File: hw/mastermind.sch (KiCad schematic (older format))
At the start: 16 parts, among them J1 CONN_01X03, SW1 R13-529, SW2 R13-529, SW3 R13-529, SW4 R13-529, U1 ESP32_THING, U2 LevelShifter

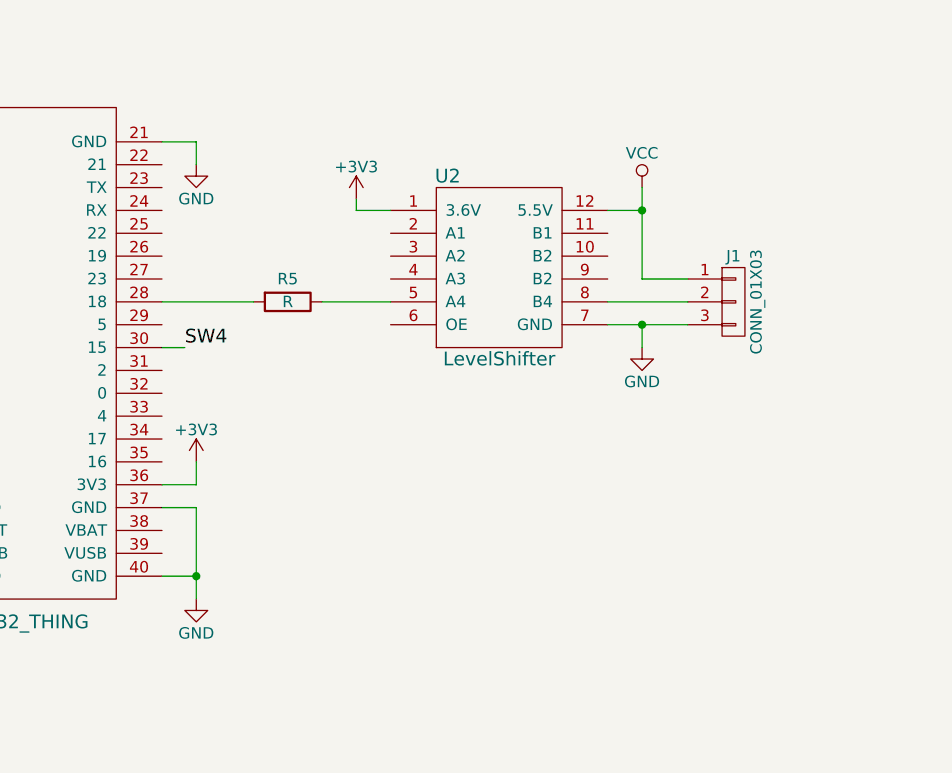
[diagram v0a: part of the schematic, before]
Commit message: Add power input header and a few corrections
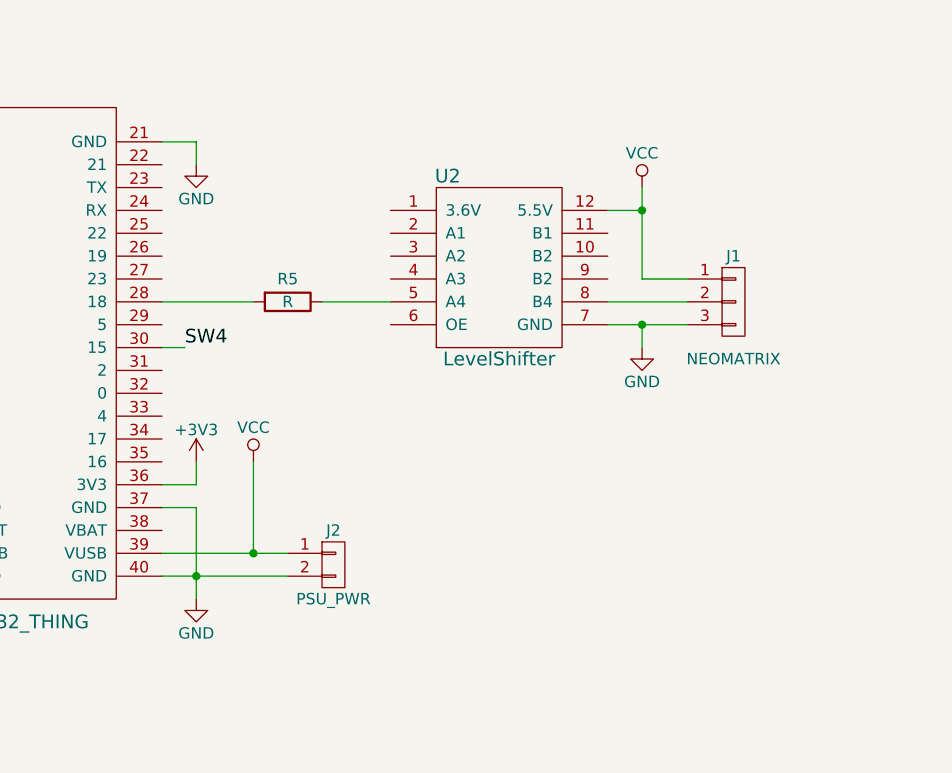
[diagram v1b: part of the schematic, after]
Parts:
- added J2: PSU_PWR, Pin_Headers:Pin_Header_Straight_1x02_Pitch2.00mm, symbol CONN_01X02
- J1: value CONN_01X03 -> NEOMATRIX
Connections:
- net +3V3: no longer U2.1 (3.6V)
- net GND: now also J2.2 (P2)
- net VCC: now also U1.39 (VUSB), J2.1 (P1)
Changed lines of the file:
@@
 $EndComp
 $Comp
-L +3V3 #PWR06
-U 1 1 59B667C6
-P 7100 3000
-F 0 "#PWR06" H 7100 2850 50  0001 C CNN
-F 1 "+3V3" H 7100 3140 50  0000 C CNN
-F 2 "" H 7100 3000 50  0001 C CNN
-F 3 "" H 7100 3000 50  0001 C CNN
-	1    7100 3000
-	1    0    0    -1
-$EndComp
-$Comp
-L GND #PWR07
+L GND #PWR06
 U 1 1 59B66A40
 P 8350 3650
-F 0 "#PWR07" H 8350 3400 50  0001 C CNN
+F 0 "#PWR06" H 8350 3400 50  0001 C CNN
 F 1 "GND" H 8350 3500 50  0000 C CNN
 F 2 "" H 8350 3650 50  0001 C CNN
@@
 $EndComp
 $Comp
-L GND #PWR08
+L GND #PWR07
 U 1 1 59B6725E
 P 4950 5100
-F 0 "#PWR08" H 4950 4850 50  0001 C CNN
+F 0 "#PWR07" H 4950 4850 50  0001 C CNN
 F 1 "GND" H 4950 4950 50  0000 C CNN
 F 2 "" H 4950 5100 50  0001 C CNN
@@
 $EndComp
 $Comp
-L +3V3 #PWR09
+L +3V3 #PWR08
 U 1 1 59B6737B
 P 4950 4250
-F 0 "#PWR09" H 4950 4100 50  0001 C CNN
+F 0 "#PWR08" H 4950 4100 50  0001 C CNN
 F 1 "+3V3" H 4950 4390 50  0000 C CNN
 F 2 "" H 4950 4250 50  0001 C CNN
@@
 $EndComp
 $Comp
-L GND #PWR010
+L GND #PWR09
 U 1 1 59B676EB
 P 6400 2850
-F 0 "#PWR010" H 6400 2600 50  0001 C CNN
+F 0 "#PWR09" H 6400 2600 50  0001 C CNN
 F 1 "GND" H 6400 2700 50  0000 C CNN
 F 2 "" H 6400 2850 50  0001 C CNN
@@
 P 8750 3450
 F 0 "J1" H 8750 3650 50  0000 C CNN
-F 1 "CONN_01X03" V 8850 3450 50  0000 C CNN
+F 1 "NEOMATRIX" H 8750 3200 50  0000 C CNN
 F 2 "Pin_Headers:Pin_Header_Straight_1x03_Pitch2.00mm" H 8750 3450 50  0001 C CNN
 F 3 "" H 8750 3450 50  0001 C CNN
@@
 $EndComp
 Wire Wire Line
-	6400 4650 6250 4650
+	6250 4650 6800 4650
 Wire Wire Line
 	6400 4350 6400 4750
@@
 Wire Wire Line
 	8350 3050 8200 3050
-Wire Wire Line
-	7250 3050 7100 3050
-Wire Wire Line
-	7100 3050 7100 3000
 Wire Wire Line
 	8350 3650 8350 3550
@@
 	4100 4850 4000 4850
 Connection ~ 4100 4150
+$Comp
+L VCC #PWR010
+U 1 1 59B7DB57
+P 6650 4150
+F 0 "#PWR010" H 6650 4000 50  0001 C CNN
+F 1 "VCC" H 6650 4300 50  0000 C CNN
+F 2 "" H 6650 4150 50  0001 C CNN
+F 3 "" H 6650 4150 50  0001 C CNN
+	1    6650 4150
+	1    0    0    -1
+$EndComp
+Wire Wire Line
+	6650 4150 6650 4550
+Wire Wire Line
+	6250 4550 6800 4550
+$Comp
+L CONN_01X02 J2
+U 1 1 59B7DDF1
+P 7000 4600
+F 0 "J2" H 7000 4750 50  0000 C CNN
+F 1 "PSU_PWR" H 7000 4450 50  0000 C CNN
+F 2 "Pin_Headers:Pin_Header_Straight_1x02_Pitch2.00mm" H 7000 4600 50  0001 C CNN
+F 3 "" H 7000 4600 50  0001 C CNN
+	1    7000 4600
+	1    0    0    -1
+$EndComp
+Connection ~ 6650 4550
 $EndSCHEMATC

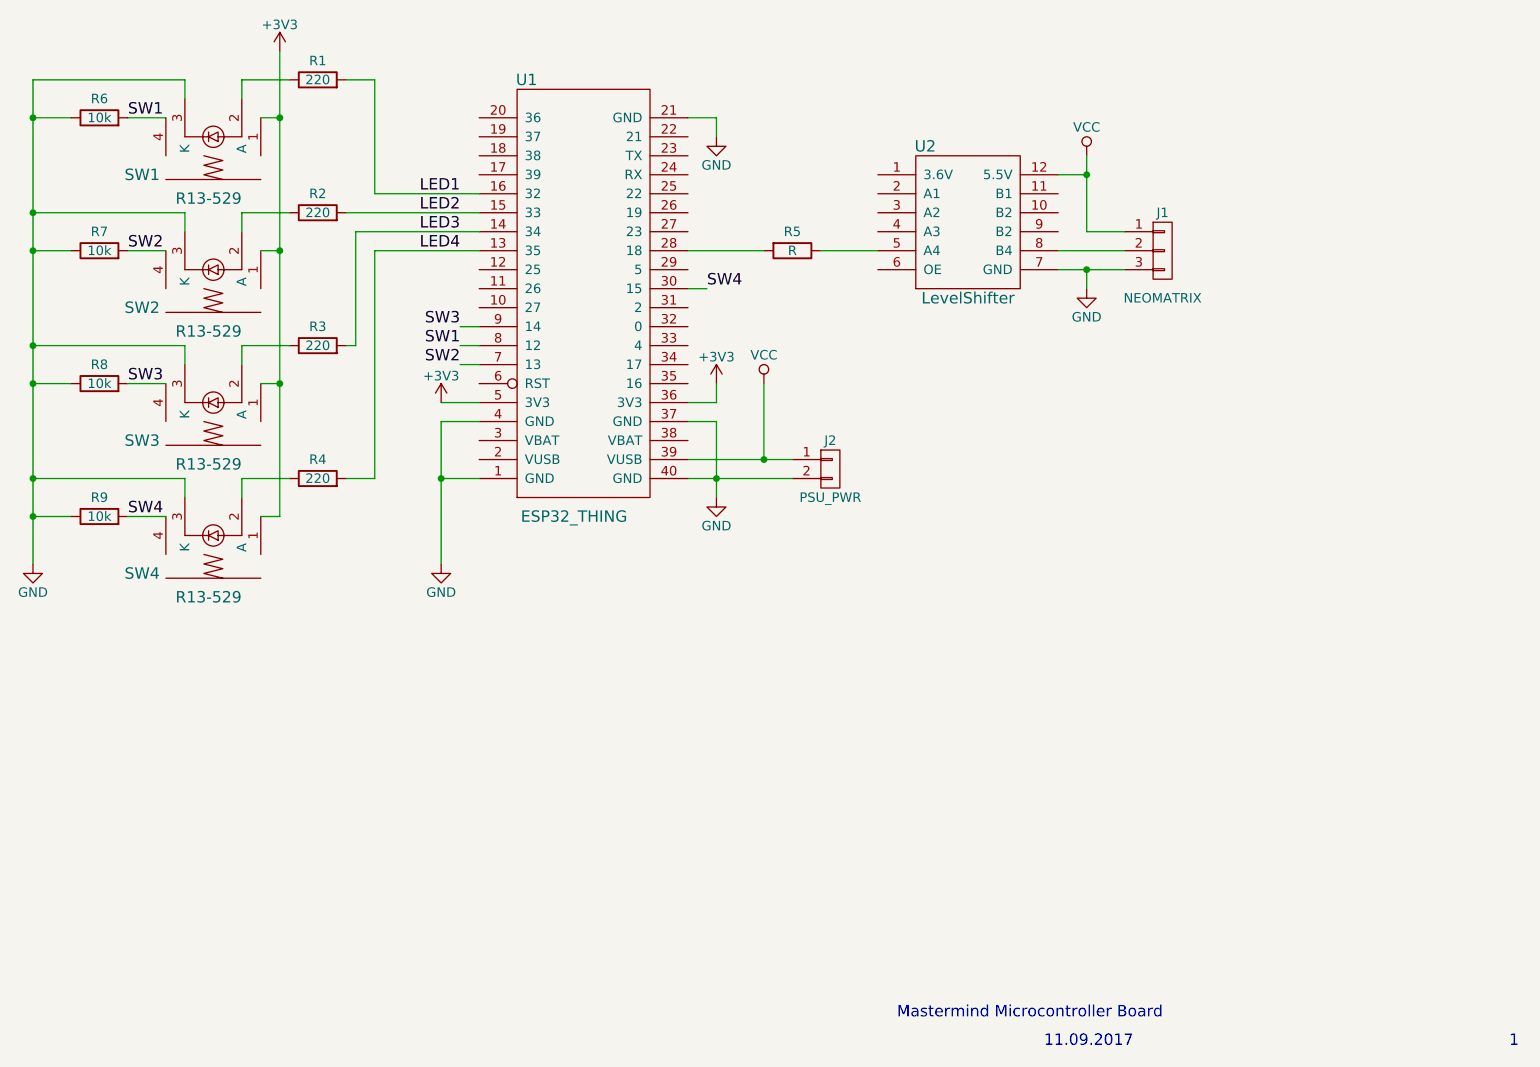
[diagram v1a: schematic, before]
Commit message: Redoing PCB design because there are a few mistakes
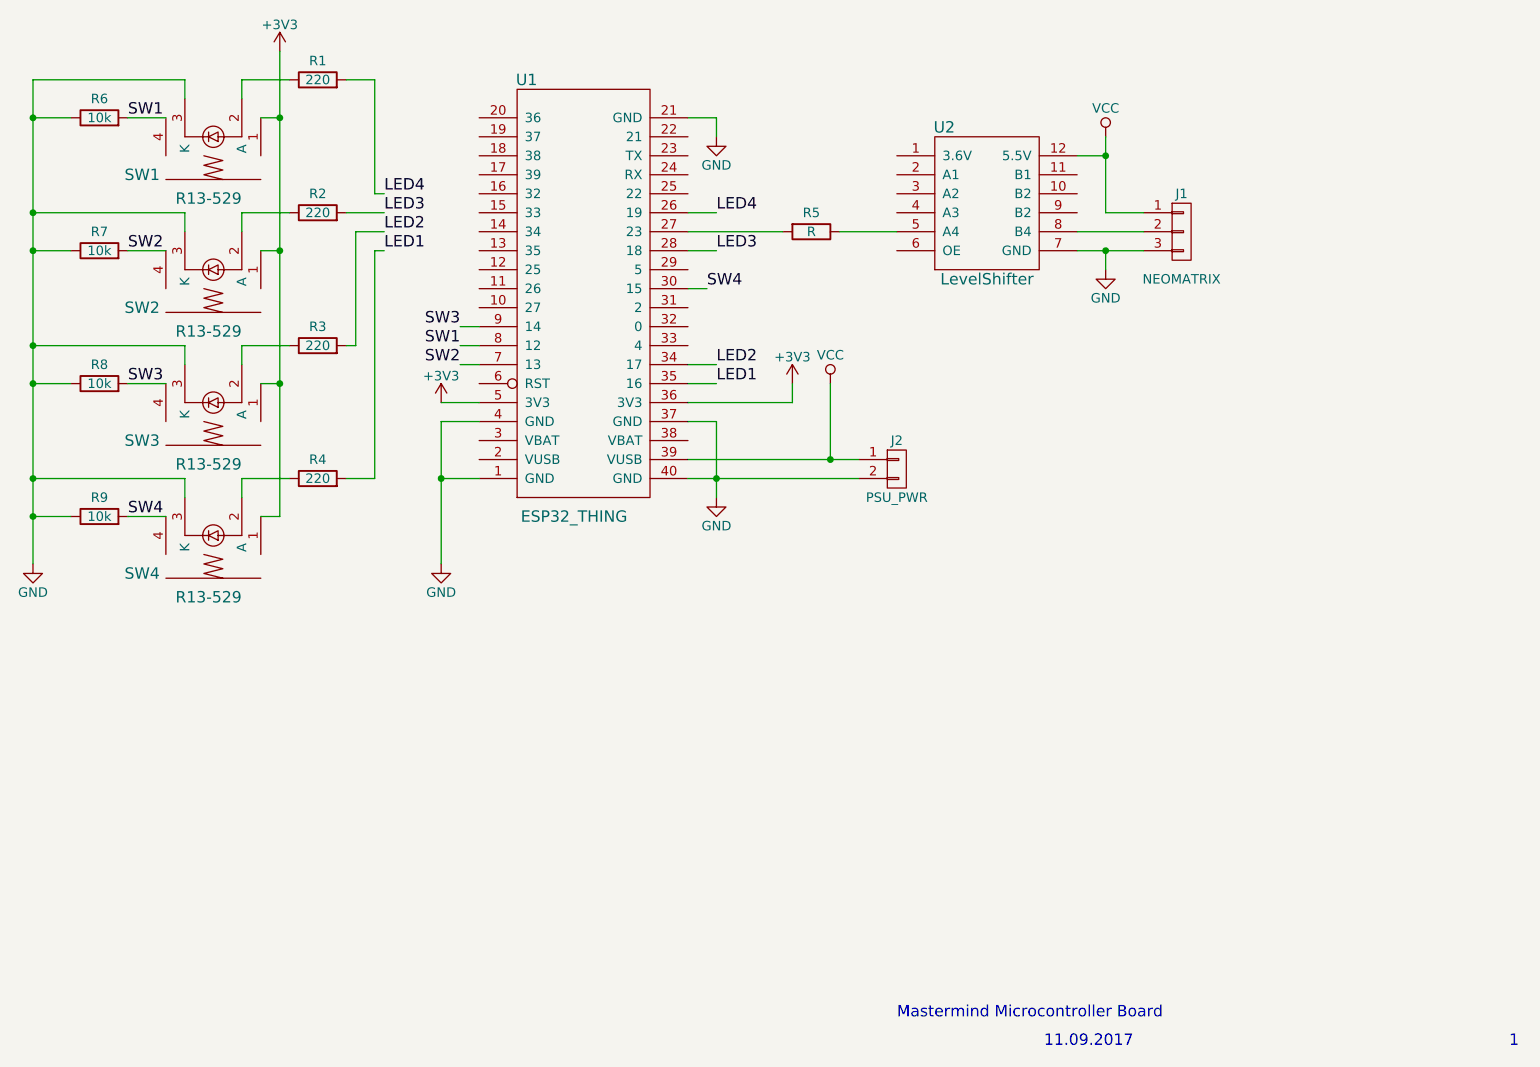
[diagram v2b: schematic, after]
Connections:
- net LED1: now also R4.2, U1.35 (16); no longer R1.2, U1.16 (32)
- net LED2: now also R3.2, U1.34 (17); no longer R2.2, U1.15 (33)
- net LED3: now also R2.2, U1.28 (18); no longer R3.2, U1.14 (34)
- net LED4: now also R1.2, U1.26 (19); no longer R4.2, U1.13 (35)
- net at U1.27 (23): now also R5.2
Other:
- moved on the sheet: J1, J2, R5, U2
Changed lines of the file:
@@
 L R R5
 U 1 1 59B65305
-P 6800 3450
-F 0 "R5" V 6700 3450 50  0000 C CNN
-F 1 "R" V 6800 3450 50  0000 C CNN
-F 2 "Resistors_THT:R_Axial_DIN0207_L6.3mm_D2.5mm_P10.16mm_Horizontal" V 6730 3450 50  0001 C CNN
-F 3 "" H 6800 3450 50  0001 C CNN
-	1    6800 3450
+P 6900 3350
+F 0 "R5" V 6800 3350 50  0000 C CNN
+F 1 "R" V 6900 3350 50  0000 C CNN
+F 2 "Resistors_THT:R_Axial_DIN0207_L6.3mm_D2.5mm_P10.16mm_Horizontal" V 6830 3350 50  0001 C CNN
+F 3 "" H 6900 3350 50  0001 C CNN
+	1    6900 3350
 	0    1    1    0
 $EndComp
@@
 L +3V3 #PWR01
 U 1 1 59B6546C
-P 6400 4150
-F 0 "#PWR01" H 6400 4000 50  0001 C CNN
-F 1 "+3V3" H 6400 4290 50  0000 C CNN
-F 2 "" H 6400 4150 50  0001 C CNN
-F 3 "" H 6400 4150 50  0001 C CNN
-	1    6400 4150
+P 6800 4150
+F 0 "#PWR01" H 6800 4000 50  0001 C CNN
+F 1 "+3V3" H 6800 4290 50  0000 C CNN
+F 2 "" H 6800 4150 50  0001 C CNN
+F 3 "" H 6800 4150 50  0001 C CNN
+	1    6800 4150
 	1    0    0    -1
 $EndComp
@@
 L VCC #PWR03
 U 1 1 59B654CC
-P 8350 2950
-F 0 "#PWR03" H 8350 2800 50  0001 C CNN
-F 1 "VCC" H 8350 3100 50  0000 C CNN
-F 2 "" H 8350 2950 50  0001 C CNN
-F 3 "" H 8350 2950 50  0001 C CNN
-	1    8350 2950
+P 8450 2850
+F 0 "#PWR03" H 8450 2700 50  0001 C CNN
+F 1 "VCC" H 8450 3000 50  0000 C CNN
+F 2 "" H 8450 2850 50  0001 C CNN
+F 3 "" H 8450 2850 50  0001 C CNN
+	1    8450 2850
 	1    0    0    -1
 $EndComp
@@
 Text Label 6350 3650 0    60   ~ 0
 SW4
-Text Label 5050 3150 2    60   ~ 0
+Text Label 4650 3450 0    60   ~ 0
 LED1
-Text Label 5050 3250 2    60   ~ 0
+Text Label 4650 3350 0    60   ~ 0
 LED2
-Text Label 5050 3350 2    60   ~ 0
+Text Label 4650 3250 0    60   ~ 0
 LED3
-Text Label 5050 3450 2    60   ~ 0
+Text Label 4650 3150 0    60   ~ 0
 LED4
 $Comp
@@
 L LevelShifter U2
 U 1 1 59B660B8
-P 7450 3650
-F 0 "U2" H 7500 4400 60  0000 C CNN
-F 1 "LevelShifter" H 7725 3600 60  0000 C CNN
-F 2 "sjf_mastermind:LevelShifter" H 7450 3650 60  0001 C CNN
-F 3 "" H 7450 3650 60  0001 C CNN
-	1    7450 3650
+P 7550 3550
+F 0 "U2" H 7600 4300 60  0000 C CNN
+F 1 "LevelShifter" H 7825 3500 60  0000 C CNN
+F 2 "sjf_mastermind:LevelShifter" H 7550 3550 60  0001 C CNN
+F 3 "" H 7550 3550 60  0001 C CNN
+	1    7550 3550
 	1    0    0    -1
 $EndComp
@@
 L GND #PWR06
 U 1 1 59B66A40
-P 8350 3650
-F 0 "#PWR06" H 8350 3400 50  0001 C CNN
-F 1 "GND" H 8350 3500 50  0000 C CNN
-F 2 "" H 8350 3650 50  0001 C CNN
-F 3 "" H 8350 3650 50  0001 C CNN
-	1    8350 3650
+P 8450 3550
+F 0 "#PWR06" H 8450 3300 50  0001 C CNN
+F 1 "GND" H 8450 3400 50  0000 C CNN
+F 2 "" H 8450 3550 50  0001 C CNN
+F 3 "" H 8450 3550 50  0001 C CNN
+	1    8450 3550
 	1    0    0    -1
 $EndComp
@@
 L CONN_01X03 J1
 U 1 1 59B6A0D5
-P 8750 3450
-F 0 "J1" H 8750 3650 50  0000 C CNN
-F 1 "NEOMATRIX" H 8750 3200 50  0000 C CNN
-F 2 "Pin_Headers:Pin_Header_Straight_1x03_Pitch2.00mm" H 8750 3450 50  0001 C CNN
-F 3 "" H 8750 3450 50  0001 C CNN
-	1    8750 3450
-	1    0    0    -1
-$EndComp
-Wire Wire Line
-	6250 4650 6800 4650
+P 8850 3350
+F 0 "J1" H 8850 3550 50  0000 C CNN
+F 1 "NEOMATRIX" H 8850 3100 50  0000 C CNN
+F 2 "Pin_Headers:Pin_Header_Straight_1x03_Pitch2.00mm" H 8850 3350 50  0001 C CNN
+F 3 "" H 8850 3350 50  0001 C CNN
+	1    8850 3350
+	1    0    0    -1
+$EndComp
+Wire Wire Line
+	6250 4650 7150 4650
 Wire Wire Line
 	6400 4350 6400 4750
 Wire Wire Line
-	6250 4250 6400 4250
-Wire Wire Line
-	6400 4250 6400 4150
+	6250 4250 6800 4250
+Wire Wire Line
+	6800 4250 6800 4150
 Wire Wire Line
 	5050 3850 5150 3850
@@
 	4600 2550 4600 3150
 Wire Wire Line
-	4600 3150 5150 3150
-Wire Wire Line
-	5150 3250 4450 3250
-Wire Wire Line
-	5150 3350 4500 3350
-Wire Wire Line
 	4500 3350 4500 3950
 Wire Wire Line
@@
 Wire Wire Line
 	4600 4650 4600 3450
-Wire Wire Line
-	4600 3450 5150 3450
 Wire Wire Line
 	3900 4750 3900 4650
@@
 Connection ~ 2800 4650
 Wire Wire Line
-	8350 2950 8350 3350
-Wire Wire Line
-	8350 3050 8200 3050
-Wire Wire Line
-	8350 3650 8350 3550
-Wire Wire Line
-	8200 3550 8550 3550
-Wire Wire Line
-	6250 3450 6650 3450
-Wire Wire Line
-	6950 3450 7250 3450
+	8450 2850 8450 3250
+Wire Wire Line
+	8450 2950 8300 2950
+Wire Wire Line
+	8450 3550 8450 3450
+Wire Wire Line
+	8300 3450 8650 3450
+Wire Wire Line
+	7050 3350 7350 3350
 Wire Wire Line
 	5150 4650 4950 4650
@@
 Wire Wire Line
 	6400 2750 6250 2750
-Connection ~ 8350 3550
-Wire Wire Line
-	8200 3450 8550 3450
-Wire Wire Line
-	8350 3350 8550 3350
-Connection ~ 8350 3050
+Connection ~ 8450 3450
+Wire Wire Line
+	8300 3350 8650 3350
+Wire Wire Line
+	8450 3250 8650 3250
+Connection ~ 8450 2950
 Text Notes 8125 7650 0    60   ~ 0
 11.09.2017
@@
 L VCC #PWR010
 U 1 1 59B7DB57
-P 6650 4150
-F 0 "#PWR010" H 6650 4000 50  0001 C CNN
-F 1 "VCC" H 6650 4300 50  0000 C CNN
-F 2 "" H 6650 4150 50  0001 C CNN
-F 3 "" H 6650 4150 50  0001 C CNN
-	1    6650 4150
-	1    0    0    -1
-$EndComp
-Wire Wire Line
-	6650 4150 6650 4550
-Wire Wire Line
-	6250 4550 6800 4550
+P 7000 4150
+F 0 "#PWR010" H 7000 4000 50  0001 C CNN
+F 1 "VCC" H 7000 4300 50  0000 C CNN
+F 2 "" H 7000 4150 50  0001 C CNN
+F 3 "" H 7000 4150 50  0001 C CNN
+	1    7000 4150
+	1    0    0    -1
+$EndComp
+Wire Wire Line
+	7000 4150 7000 4550
+Wire Wire Line
+	6250 4550 7150 4550
 $Comp
 L CONN_01X02 J2
 U 1 1 59B7DDF1
-P 7000 4600
-F 0 "J2" H 7000 4750 50  0000 C CNN
-F 1 "PSU_PWR" H 7000 4450 50  0000 C CNN
-F 2 "Pin_Headers:Pin_Header_Straight_1x02_Pitch2.00mm" H 7000 4600 50  0001 C CNN
-F 3 "" H 7000 4600 50  0001 C CNN
-	1    7000 4600
-	1    0    0    -1
-$EndComp
-Connection ~ 6650 4550
+P 7350 4600
+F 0 "J2" H 7350 4750 50  0000 C CNN
+F 1 "PSU_PWR" H 7350 4450 50  0000 C CNN
+F 2 "Pin_Headers:Pin_Header_Straight_1x02_Pitch2.00mm" H 7350 4600 50  0001 C CNN
+F 3 "" H 7350 4600 50  0001 C CNN
+	1    7350 4600
+	1    0    0    -1
+$EndComp
+Connection ~ 7000 4550
+Wire Wire Line
+	4600 3150 4650 3150
+Wire Wire Line
+	4650 3250 4450 3250
+Wire Wire Line
+	4500 3350 4650 3350
+Wire Wire Line
+	4600 3450 4650 3450
+Text Label 6400 4150 0    60   ~ 0
+LED1
+Text Label 6400 4050 0    60   ~ 0
+LED2
+Text Label 6400 3450 0    60   ~ 0
+LED3
+Text Label 6400 3250 0    60   ~ 0
+LED4
+Wire Wire Line
+	6400 3250 6250 3250
+Wire Wire Line
+	6250 3450 6400 3450
+Wire Wire Line
+	6400 4050 6250 4050
+Wire Wire Line
+	6250 4150 6400 4150
+Wire Wire Line
+	6750 3350 6250 3350
 $EndSCHEMATC
